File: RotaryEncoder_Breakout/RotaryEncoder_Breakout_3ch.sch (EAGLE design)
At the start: 8 parts

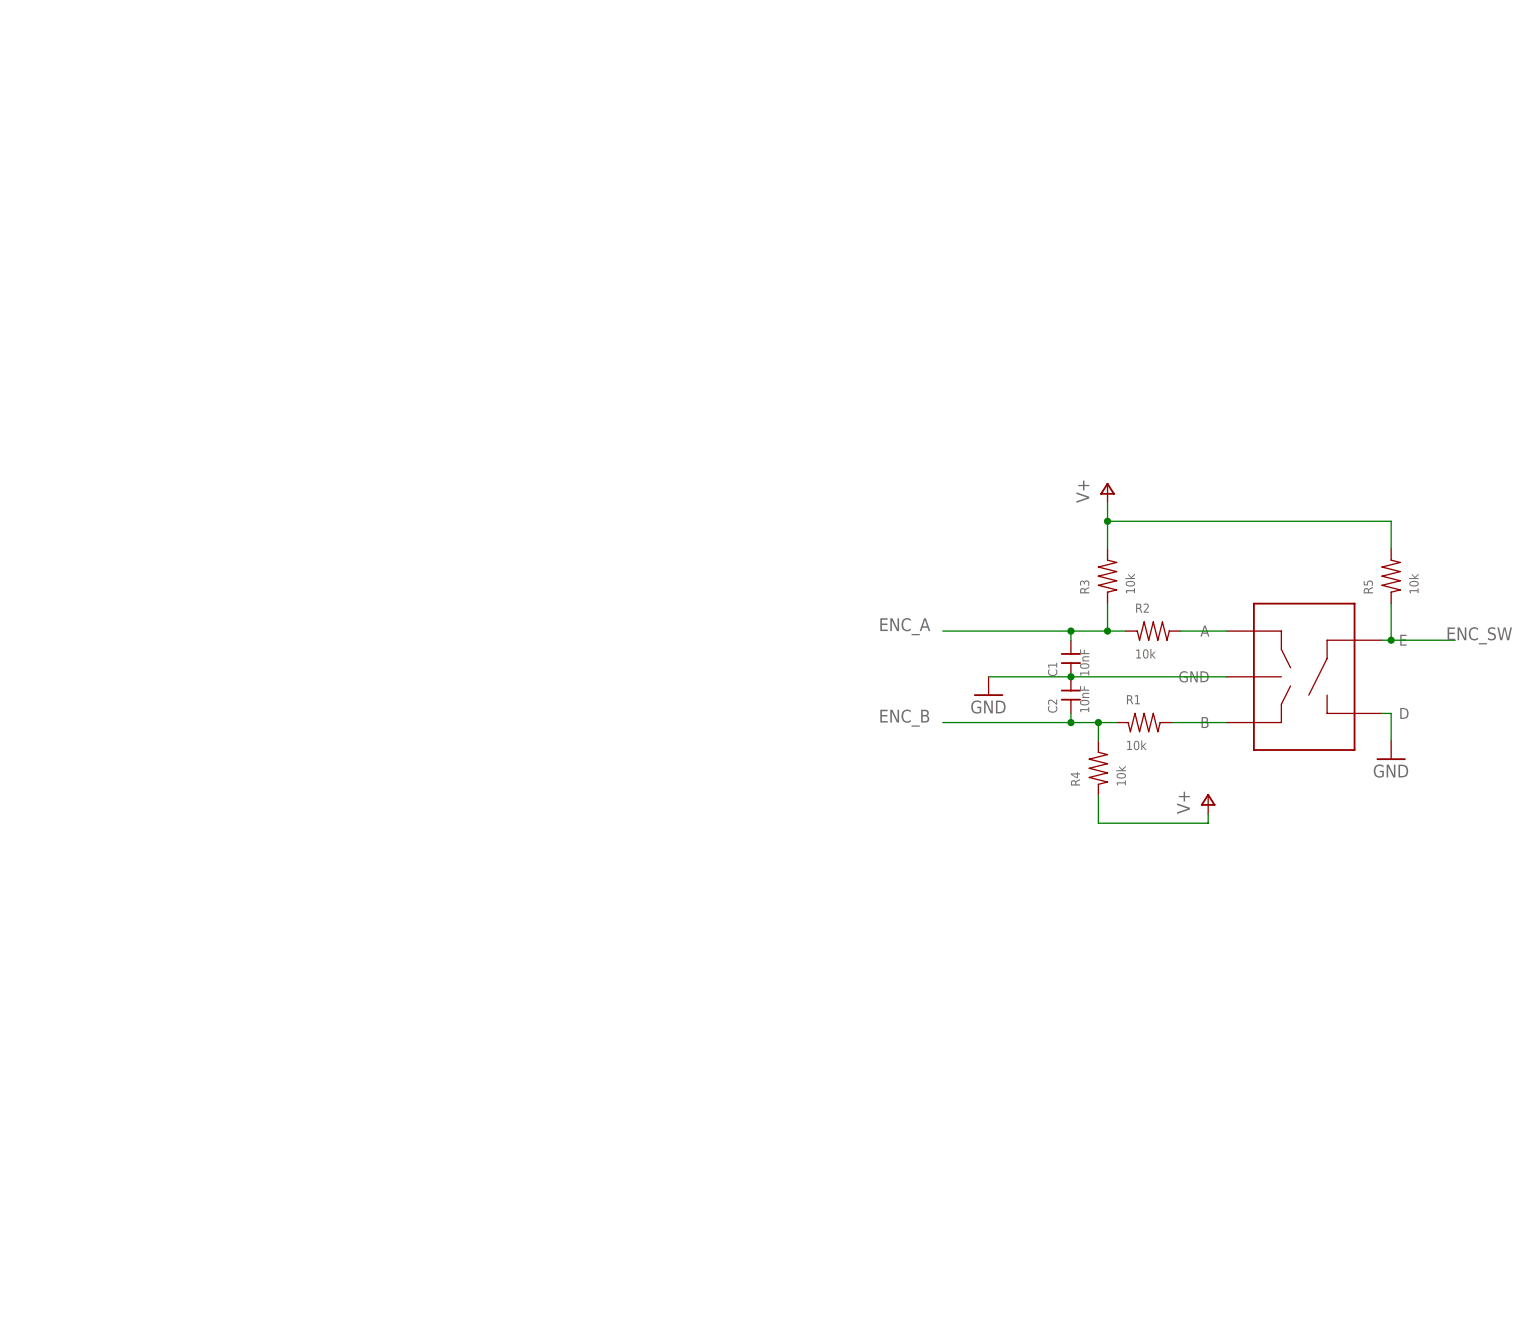
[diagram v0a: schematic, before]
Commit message: 3 and 4 channel rotary encoder board; still need to sort out data signals sent off-board
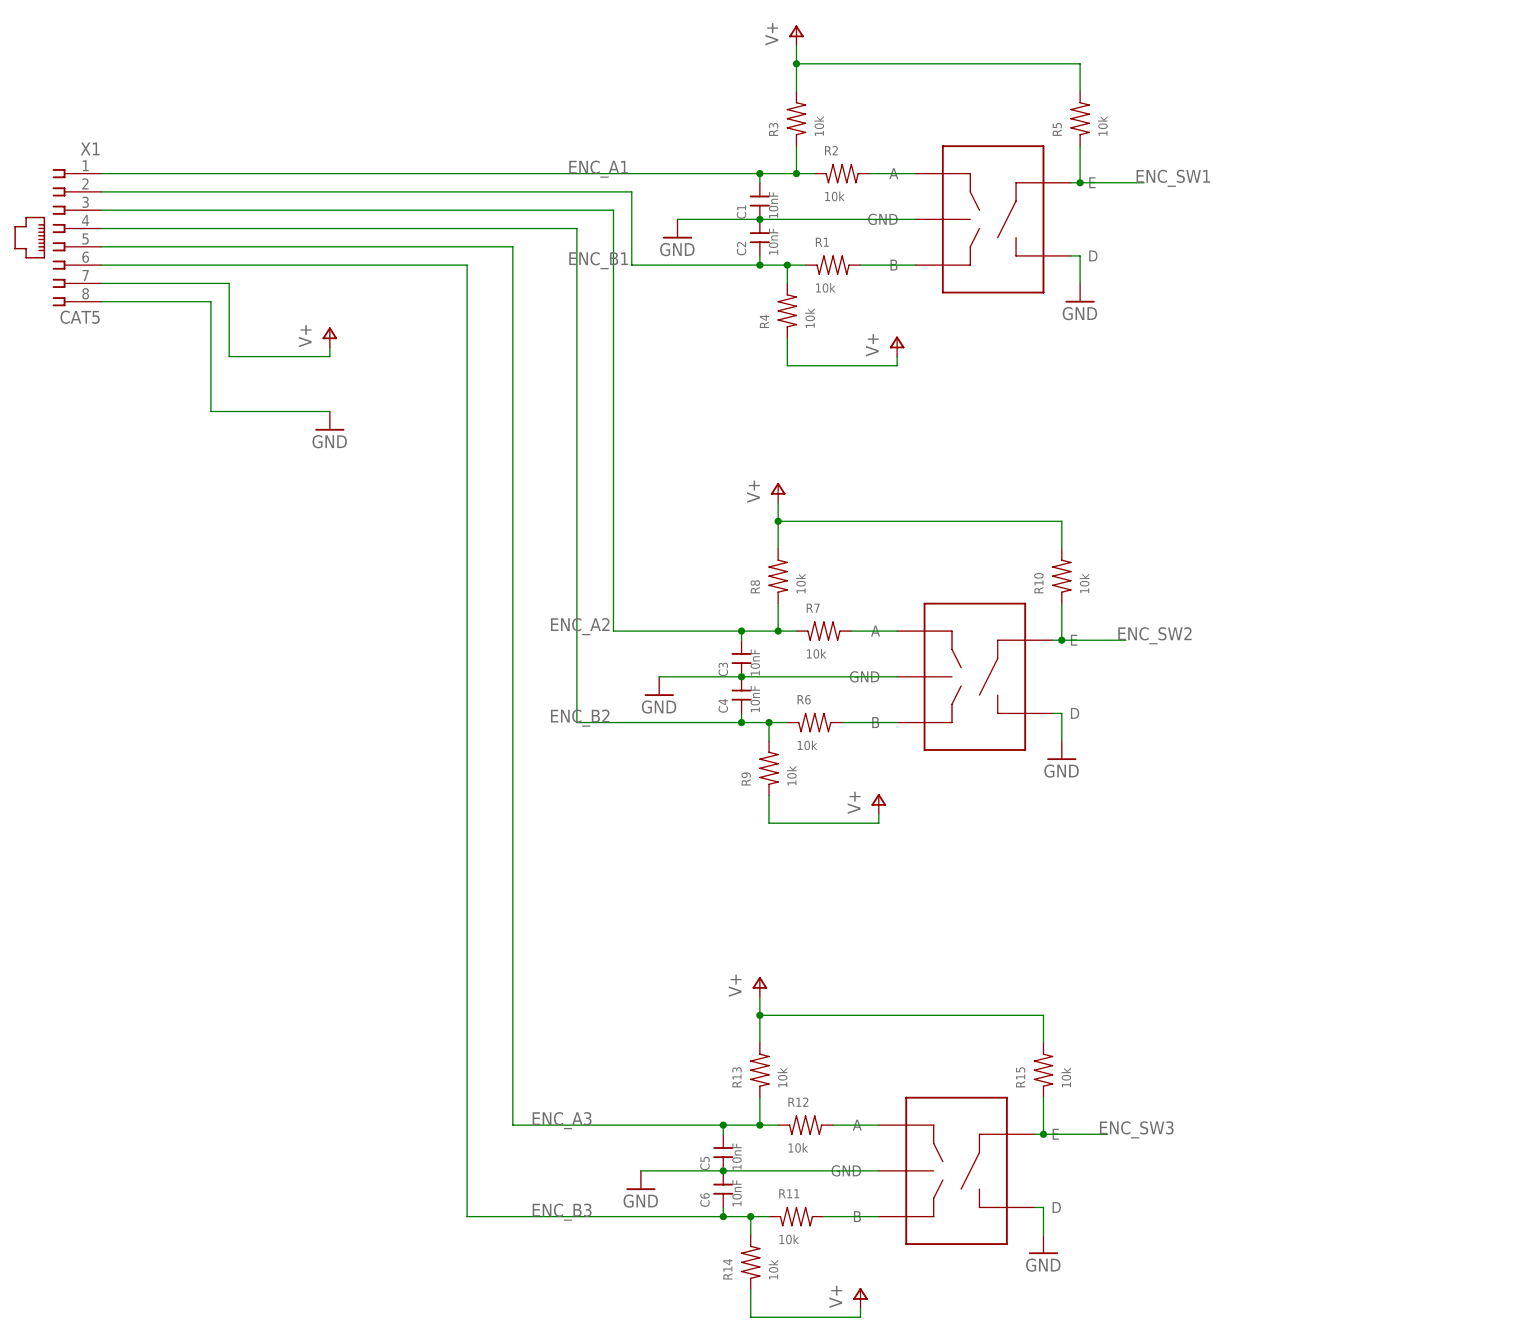
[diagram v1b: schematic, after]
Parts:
- added C3, C4, C5, C6: 10nF, rlc-jqi:CAP0603
- added ENC2, ENC3: PEC09, connector-jqi:PEC09
- added R10, R11, R12, R13, R14, R15, R6, R7, R8, R9: 10k, rlc-jqi:RES0603
- added X1: CAT5, connector-jqi:CAT5
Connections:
- net ENC_SW renamed ENC_SW1
- removed net ENC_A: C1.P$2, R2.P$1, R3.P$1
- removed net ENC_B: C2.P$1, R1.P$1, R4.P$2
- new net ENC_A1: C1.P$2, R2.P$1, R3.P$1, X1.1
- new net ENC_A2: C3.P$2, R7.P$1, R8.P$1, X1.3
- new net ENC_A3: C5.P$2, R12.P$1, R13.P$1, X1.5
- new net ENC_B1: C2.P$1, R1.P$1, R4.P$2, X1.2
- new net ENC_B2: C4.P$1, R6.P$1, R9.P$2, X1.4
- new net ENC_B3: C6.P$1, R11.P$1, R14.P$2, X1.6
- new net ENC_SW2: ENC2.E, R10.P$1
- new net ENC_SW3: ENC3.E, R15.P$1
- new net N$1: ENC2.B, R6.P$2
- new net N$2: ENC2.A, R7.P$2
- new net N$3: ENC3.B, R11.P$2
- new net N$6: ENC3.A, R12.P$2
- net GND: now also C3.P$1, C4.P$2, C5.P$1, C6.P$2, ENC2.D, ENC2.GND, ENC3.D, ENC3.GND, X1.8
- net V+: now also R10.P$2, R13.P$2, R14.P$1, R15.P$2, R8.P$2, R9.P$1, X1.7
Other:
- moved on the sheet: C1, C2, R1, R2, R3, R4, R5
